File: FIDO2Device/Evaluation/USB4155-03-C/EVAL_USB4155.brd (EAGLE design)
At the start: 30 x 30 mm, 6 parts, among them CN1 USB4155-03-C, CN2 87520-0010BLF, CN3 IF_5PIN_H

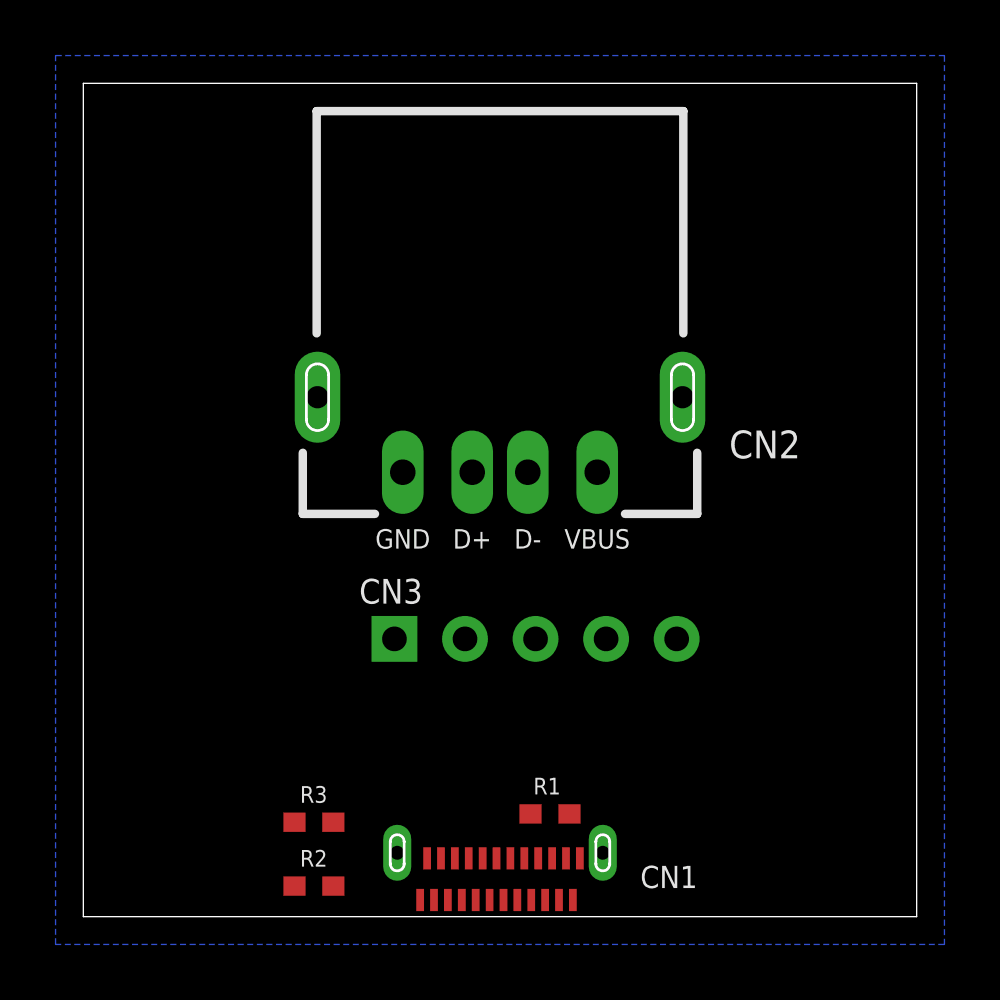
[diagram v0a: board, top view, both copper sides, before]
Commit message: レイアウトを更新
・信号線のViaを仮配置
・デザインルールを一部修正
（Drill＝0.2mm、Restring＝0.1mm、Clearance＝0.15mm）
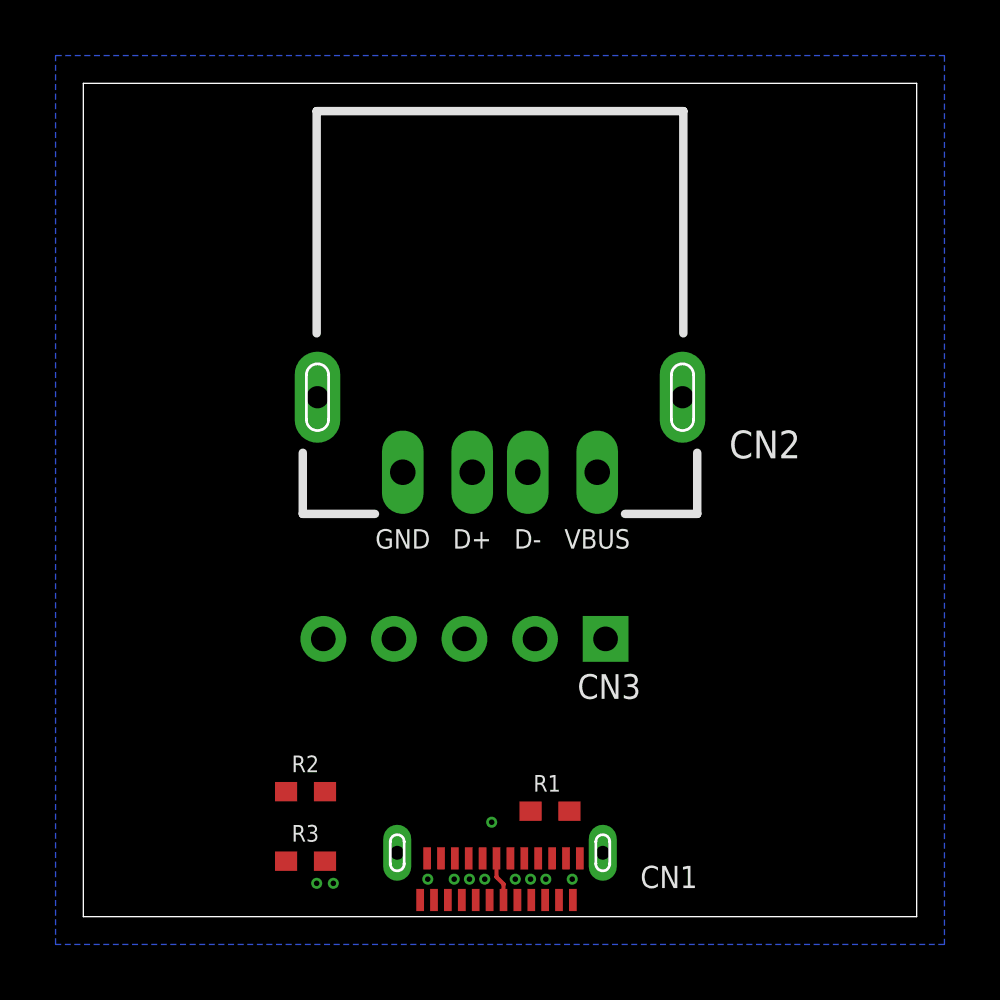
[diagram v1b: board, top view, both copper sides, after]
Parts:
- moved CN3 7.60 mm to (18.8, 10.0), turned to 180 degrees
- moved R2 3.41 mm to (8.00, 4.50), turned to 180 degrees
- moved R3 1.43 mm to (8.00, 2.00)
- moved R1 0.10 mm to (16.8, 3.80)
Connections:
- net N$1 renamed CC_1
- net N$2 renamed CC_2
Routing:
- net DN_C: track 0.00 -> 1.60 mm
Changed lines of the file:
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@@
 <param name="mtCopper" value="0.035mm 0.0175mm 0.035mm 0.035mm 0.035mm 0.035mm 0.035mm 0.035mm 0.035mm 0.035mm 0.035mm 0.035mm 0.035mm 0.035mm 0.0175mm 0.035mm"/>
 <param name="mtIsolate" value="1.5mm 1.1mm 0.2mm 0.15mm 0.2mm 0.15mm 0.2mm 0.15mm 0.2mm 0.15mm 0.2mm 0.15mm 0.2mm 0.15mm 0.2mm"/>
-<param name="mdWireWire" value="6mil"/>
-<param name="mdWirePad" value="6mil"/>
-<param name="mdWireVia" value="6mil"/>
-<param name="mdPadPad" value="6mil"/>
-<param name="mdPadVia" value="6mil"/>
-<param name="mdViaVia" value="6mil"/>
+<param name="mdWireWire" value="0.15mm"/>
+<param name="mdWirePad" value="0.15mm"/>
+<param name="mdWireVia" value="0.15mm"/>
+<param name="mdPadPad" value="0.15mm"/>
+<param name="mdPadVia" value="0.15mm"/>
+<param name="mdViaVia" value="0.15mm"/>
 <param name="mdSmdPad" value="0mil"/>
 <param name="mdSmdVia" value="0mil"/>
@@
 <param name="mdSmdStop" value="0mil"/>
 <param name="msWidth" value="6mil"/>
-<param name="msDrill" value="12mil"/>
+<param name="msDrill" value="0.2mm"/>
 <param name="msMicroVia" value="12mil"/>
 <param name="msBlindViaRatio" value="0.5"/>
@@
 <param name="rlMinPadBottom" value="10mil"/>
 <param name="rlMaxPadBottom" value="20mil"/>
-<param name="rlMinViaOuter" value="6mil"/>
+<param name="rlMinViaOuter" value="0.1mm"/>
 <param name="rlMaxViaOuter" value="20mil"/>
-<param name="rlMinViaInner" value="6mil"/>
+<param name="rlMinViaInner" value="0.1mm"/>
 <param name="rlMaxViaInner" value="20mil"/>
 <param name="rlMinMicroViaOuter" value="4mil"/>
@@
 </element>
 <element name="CN2" library="Connectors" package="87520-0010BLF" value="87520-0010BLF" x="15" y="16"/>
-<element name="CN3" library="Connectors" package="HEADER_5PIN" value="IF_5PIN_H" x="11.2" y="10"/>
-<element name="R1" library="Parts" package="R0402N" value="5.1k" x="16.8" y="3.7" smashed="yes" rot="R180">
-<attribute name="NAME" x="16.2" y="4.4" size="0.6" layer="25"/>
-<attribute name="VALUE" x="17.3" y="5" size="0.6" layer="27" rot="R180"/>
-</element>
-<element name="R2" library="Parts" package="R0402N" value="5.1k" x="8.3" y="1.1" smashed="yes">
-<attribute name="NAME" x="7.8" y="1.8" size="0.6" layer="25"/>
-<attribute name="VALUE" x="7.8" y="-0.2" size="0.6" layer="27"/>
-</element>
-<element name="R3" library="Parts" package="R0402N" value="0" x="8.3" y="3.4" smashed="yes">
-<attribute name="NAME" x="7.8" y="4.1" size="0.6" layer="25"/>
-<attribute name="VALUE" x="7.8" y="2.1" size="0.6" layer="27"/>
+<element name="CN3" library="Connectors" package="HEADER_5PIN" value="IF_5PIN_H" x="18.8" y="10" rot="R180"/>
+<element name="R1" library="Parts" package="R0402N" value="5.1k" x="16.8" y="3.8" smashed="yes" rot="R180">
+<attribute name="NAME" x="16.2" y="4.5" size="0.6" layer="25"/>
+<attribute name="VALUE" x="17.3" y="5.1" size="0.6" layer="27" rot="R180"/>
+</element>
+<element name="R2" library="Parts" package="R0402N" value="5.1k" x="8" y="4.5" smashed="yes" rot="R180">
+<attribute name="NAME" x="7.5" y="5.2" size="0.6" layer="25"/>
+<attribute name="VALUE" x="8.5" y="5.8" size="0.6" layer="27" rot="R180"/>
+</element>
+<element name="R3" library="Parts" package="R0402N" value="0" x="8" y="2" smashed="yes">
+<attribute name="NAME" x="7.5" y="2.7" size="0.6" layer="25"/>
+<attribute name="VALUE" x="7.5" y="0.7" size="0.6" layer="27"/>
 </element>
 </elements>
@@
 <vertex x="-1" y="-1"/>
 </polygon>
-<wire x1="17.625" y1="0.6" x2="17.875" y2="2.1" width="0" layer="19" extent="1-1"/>
-<wire x1="17.5" y1="3.7" x2="17.875" y2="2.1" width="0" layer="19" extent="1-1"/>
-<wire x1="12.375" y1="2.1" x2="17.5" y2="3.7" width="0" layer="19" extent="1-1"/>
-<wire x1="12.125" y1="0.6" x2="12.375" y2="2.1" width="0" layer="19" extent="1-1"/>
-<wire x1="7.6" y1="1.1" x2="12.125" y2="0.6" width="0" layer="19" extent="1-1"/>
-<wire x1="11.2" y1="10" x2="12.375" y2="2.1" width="0" layer="19" extent="1-1"/>
+<via x="17.6" y="1.35" extent="1-16" drill="0.2"/>
+<via x="12.4" y="1.35" extent="1-16" drill="0.2"/>
+<wire x1="17.6" y1="1.35" x2="17.875" y2="2.1" width="0" layer="19" extent="1-1"/>
+<wire x1="17.625" y1="0.6" x2="17.6" y2="1.35" width="0" layer="19" extent="1-1"/>
+<wire x1="12.375" y1="2.1" x2="12.4" y2="1.35" width="0" layer="19" extent="1-1"/>
+<wire x1="12.125" y1="0.6" x2="12.4" y2="1.35" width="0" layer="19" extent="1-1"/>
+<wire x1="17.5" y1="3.8" x2="17.875" y2="2.1" width="0" layer="19" extent="1-1"/>
+<wire x1="8.7" y1="4.5" x2="12.375" y2="2.1" width="0" layer="19" extent="1-1"/>
 </signal>
 <signal name="DP_C">
@@
 <contactref element="CN1" pad="A6"/>
 <contactref element="CN1" pad="B6"/>
-<wire x1="16.28" y1="10" x2="14" y2="16" width="0" layer="19" extent="1-1"/>
-<wire x1="15.375" y1="2.1" x2="16.28" y2="10" width="0" layer="19" extent="1-1"/>
-<wire x1="14.625" y1="0.6" x2="15.375" y2="2.1" width="0" layer="19" extent="1-1"/>
+<via x="15.55" y="1.35" extent="1-16" drill="0.2"/>
+<via x="14.45" y="1.35" extent="1-16" drill="0.2"/>
+<via x="14.7" y="3.4" extent="1-16" drill="0.2"/>
+<wire x1="13.72" y1="10" x2="14" y2="16" width="0" layer="19" extent="1-1"/>
+<wire x1="14.7" y1="3.4" x2="13.72" y2="10" width="0" layer="19" extent="1-1"/>
+<wire x1="15.375" y1="2.1" x2="14.7" y2="3.4" width="0" layer="19" extent="1-1"/>
+<wire x1="15.55" y1="1.35" x2="15.375" y2="2.1" width="0" layer="19" extent="1-1"/>
+<wire x1="14.45" y1="1.35" x2="15.55" y2="1.35" width="0" layer="19" extent="1-1"/>
+<wire x1="14.625" y1="0.6" x2="14.45" y2="1.35" width="0" layer="19" extent="1-1"/>
 </signal>
 <signal name="DN_C">
@@
 <contactref element="CN1" pad="A7"/>
 <contactref element="CN1" pad="B7"/>
-<wire x1="13.74" y1="10" x2="16" y2="16" width="0" layer="19" extent="1-1"/>
-<wire x1="14.875" y1="2.1" x2="13.74" y2="10" width="0" layer="19" extent="1-1"/>
-<wire x1="15.125" y1="0.6" x2="14.875" y2="2.1" width="0" layer="19" extent="1-1"/>
+<wire x1="15.125" y1="0.6" x2="15.125" y2="1.175" width="0.1524" layer="1"/>
+<wire x1="14.875" y1="2.1" x2="14.875" y2="1.425" width="0.1524" layer="1"/>
+<wire x1="14.875" y1="1.425" x2="15.125" y2="1.175" width="0.1524" layer="1"/>
+<wire x1="16.26" y1="10" x2="16" y2="16" width="0" layer="19" extent="1-1"/>
+<wire x1="14.875" y1="2.1" x2="16.26" y2="10" width="0" layer="19" extent="1-1"/>
 </signal>
 <signal name="VBUS_C">
@@
 <contactref element="CN1" pad="A9"/>
 <contactref element="CN1" pad="B4"/>
-<wire x1="18.82" y1="10" x2="18.5" y2="16" width="0" layer="19" extent="1-1"/>
-<wire x1="16.375" y1="2.1" x2="18.82" y2="10" width="0" layer="19" extent="1-1"/>
-<wire x1="16.125" y1="0.6" x2="16.375" y2="2.1" width="0" layer="19" extent="1-1"/>
-<wire x1="13.875" y1="2.1" x2="16.375" y2="2.1" width="0" layer="19" extent="1-1"/>
-<wire x1="13.625" y1="0.6" x2="13.875" y2="2.1" width="0" layer="19" extent="1-1"/>
+<via x="13.35" y="1.35" extent="1-16" drill="0.2"/>
+<via x="16.65" y="1.35" extent="1-16" drill="0.2"/>
+<wire x1="11.18" y1="10" x2="18.5" y2="16" width="0" layer="19" extent="1-1"/>
+<wire x1="13.875" y1="2.1" x2="11.18" y2="10" width="0" layer="19" extent="1-1"/>
+<wire x1="13.35" y1="1.35" x2="13.875" y2="2.1" width="0" layer="19" extent="1-1"/>
+<wire x1="13.625" y1="0.6" x2="13.35" y2="1.35" width="0" layer="19" extent="1-1"/>
+<wire x1="16.375" y1="2.1" x2="13.875" y2="2.1" width="0" layer="19" extent="1-1"/>
+<wire x1="16.65" y1="1.35" x2="16.375" y2="2.1" width="0" layer="19" extent="1-1"/>
+<wire x1="16.125" y1="0.6" x2="16.65" y2="1.35" width="0" layer="19" extent="1-1"/>
 </signal>
 <signal name="FG_C">
@@
 <contactref element="CN1" pad="FG1"/>
 <contactref element="CN1" pad="FG2"/>
-<wire x1="21.36" y1="10" x2="21.57" y2="18.7" width="0" layer="19" extent="1-1"/>
-<wire x1="18.7" y1="2.3" x2="21.36" y2="10" width="0" layer="19" extent="1-1"/>
-<wire x1="11.3" y1="2.3" x2="18.7" y2="2.3" width="0" layer="19" extent="1-1"/>
 <wire x1="8.43" y1="18.7" x2="21.57" y2="18.7" width="0" layer="19" extent="1-1"/>
-</signal>
-<signal name="N$1">
+<wire x1="8.64" y1="10" x2="8.43" y2="18.7" width="0" layer="19" extent="1-1"/>
+<wire x1="11.3" y1="2.3" x2="8.64" y2="10" width="0" layer="19" extent="1-1"/>
+<wire x1="18.7" y1="2.3" x2="11.3" y2="2.3" width="0" layer="19" extent="1-1"/>
+</signal>
+<signal name="CC_1">
 <contactref element="CN1" pad="A5"/>
 <contactref element="R3" pad="2"/>
 <contactref element="R1" pad="2"/>
-<wire x1="15.875" y1="2.1" x2="16.1" y2="3.7" width="0" layer="19" extent="1-1"/>
-<wire x1="9" y1="3.4" x2="15.875" y2="2.1" width="0" layer="19" extent="1-1"/>
-</signal>
-<signal name="N$2">
+<via x="16.1" y="1.35" extent="1-16" drill="0.2"/>
+<via x="9" y="1.2" extent="1-16" drill="0.2"/>
+<wire x1="15.875" y1="2.1" x2="16.1" y2="3.8" width="0" layer="19" extent="1-1"/>
+<wire x1="16.1" y1="1.35" x2="15.875" y2="2.1" width="0" layer="19" extent="1-1"/>
+<wire x1="9" y1="1.2" x2="15.875" y2="2.1" width="0" layer="19" extent="1-1"/>
+<wire x1="8.7" y1="2" x2="9" y2="1.2" width="0" layer="19" extent="1-1"/>
+</signal>
+<signal name="CC_2">
 <contactref element="CN1" pad="B5"/>
 <contactref element="R2" pad="2"/>
 <contactref element="R3" pad="1"/>
-<wire x1="9" y1="1.1" x2="14.125" y2="0.6" width="0" layer="19" extent="1-1"/>
-<wire x1="7.6" y1="3.4" x2="9" y2="1.1" width="0" layer="19" extent="1-1"/>
+<via x="13.9" y="1.35" extent="1-16" drill="0.2"/>
+<via x="8.4" y="1.2" extent="1-16" drill="0.2"/>
+<wire x1="13.9" y1="1.35" x2="14.125" y2="0.6" width="0" layer="19" extent="1-1"/>
+<wire x1="8.4" y1="1.2" x2="13.9" y2="1.35" width="0" layer="19" extent="1-1"/>
+<wire x1="7.3" y1="2" x2="8.4" y2="1.2" width="0" layer="19" extent="1-1"/>
+<wire x1="7.3" y1="4.5" x2="7.3" y2="2" width="0" layer="19" extent="1-1"/>
 </signal>
 </signals>

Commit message: レイアウトを更新
・差動信号を配線
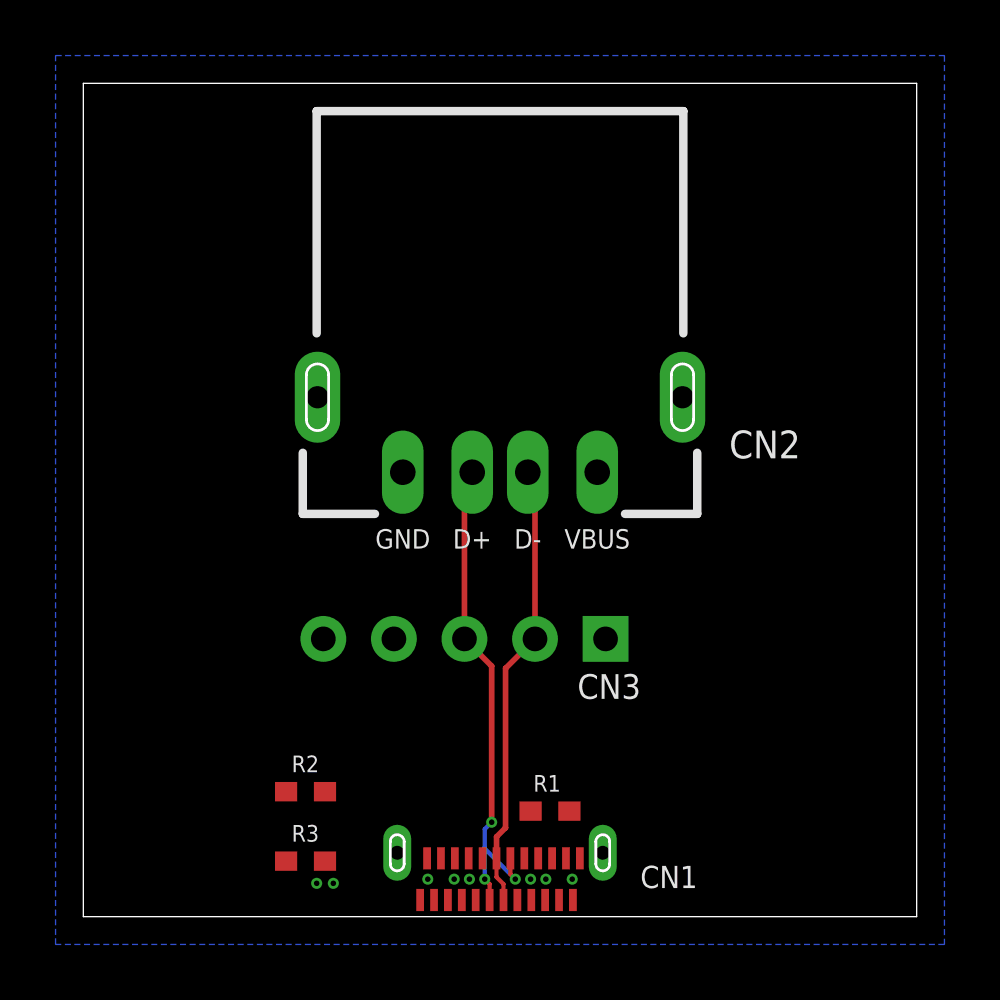
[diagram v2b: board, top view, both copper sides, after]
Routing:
- net DP_C: track 0.00 -> 18.5 mm
- net DN_C: track 1.60 -> 16.2 mm
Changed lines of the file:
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@@
 <via x="14.45" y="1.35" extent="1-16" drill="0.2"/>
 <via x="14.7" y="3.4" extent="1-16" drill="0.2"/>
-<wire x1="13.72" y1="10" x2="14" y2="16" width="0" layer="19" extent="1-1"/>
-<wire x1="14.7" y1="3.4" x2="13.72" y2="10" width="0" layer="19" extent="1-1"/>
-<wire x1="15.375" y1="2.1" x2="14.7" y2="3.4" width="0" layer="19" extent="1-1"/>
-<wire x1="15.55" y1="1.35" x2="15.375" y2="2.1" width="0" layer="19" extent="1-1"/>
-<wire x1="14.45" y1="1.35" x2="15.55" y2="1.35" width="0" layer="19" extent="1-1"/>
-<wire x1="14.625" y1="0.6" x2="14.45" y2="1.35" width="0" layer="19" extent="1-1"/>
+<wire x1="14.625" y1="0.6" x2="14.625" y2="1.175" width="0.1524" layer="1"/>
+<wire x1="15.55" y1="1.35" x2="15.375" y2="1.525" width="0.1524" layer="1"/>
+<wire x1="15.375" y1="1.525" x2="15.375" y2="2.1" width="0.1524" layer="1"/>
+<wire x1="14.45" y1="1.35" x2="14.625" y2="1.175" width="0.1524" layer="1"/>
+<wire x1="14.7" y1="3.4" x2="14.7" y2="9.02" width="0.2032" layer="1"/>
+<wire x1="14.7" y1="9.02" x2="13.72" y2="10" width="0.2032" layer="1"/>
+<wire x1="14.7" y1="3.4" x2="14.45" y2="3.15" width="0.1524" layer="16"/>
+<wire x1="14.45" y1="3.15" x2="14.45" y2="2.5" width="0.1524" layer="16"/>
+<wire x1="14.45" y1="2.45" x2="14.45" y2="1.35" width="0.1524" layer="16"/>
+<wire x1="15.55" y1="1.35" x2="14.45" y2="2.45" width="0.1524" layer="16"/>
+<wire x1="14.45" y1="2.45" x2="14.45" y2="2.5" width="0.1524" layer="16"/>
+<wire x1="13.72" y1="10" x2="13.72" y2="15.72" width="0.2032" layer="1"/>
+<wire x1="13.72" y1="15.72" x2="14" y2="16" width="0.2032" layer="1"/>
 </signal>
 <signal name="DN_C">
@@
 <wire x1="14.875" y1="2.1" x2="14.875" y2="1.425" width="0.1524" layer="1"/>
 <wire x1="14.875" y1="1.425" x2="15.125" y2="1.175" width="0.1524" layer="1"/>
-<wire x1="16.26" y1="10" x2="16" y2="16" width="0" layer="19" extent="1-1"/>
-<wire x1="14.875" y1="2.1" x2="16.26" y2="10" width="0" layer="19" extent="1-1"/>
+<wire x1="14.875" y1="2.1" x2="14.875" y2="2.875" width="0.2032" layer="1"/>
+<wire x1="14.875" y1="2.875" x2="15.2" y2="3.2" width="0.2032" layer="1"/>
+<wire x1="15.2" y1="3.2" x2="15.2" y2="8.94" width="0.2032" layer="1"/>
+<wire x1="15.2" y1="8.94" x2="16.26" y2="10" width="0.2032" layer="1"/>
+<wire x1="16.26" y1="10" x2="16.26" y2="15.74" width="0.2032" layer="1"/>
+<wire x1="16.26" y1="15.74" x2="16" y2="16" width="0.2032" layer="1"/>
 </signal>
 <signal name="VBUS_C">

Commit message: レイアウトを更新
・電源／信号を配線
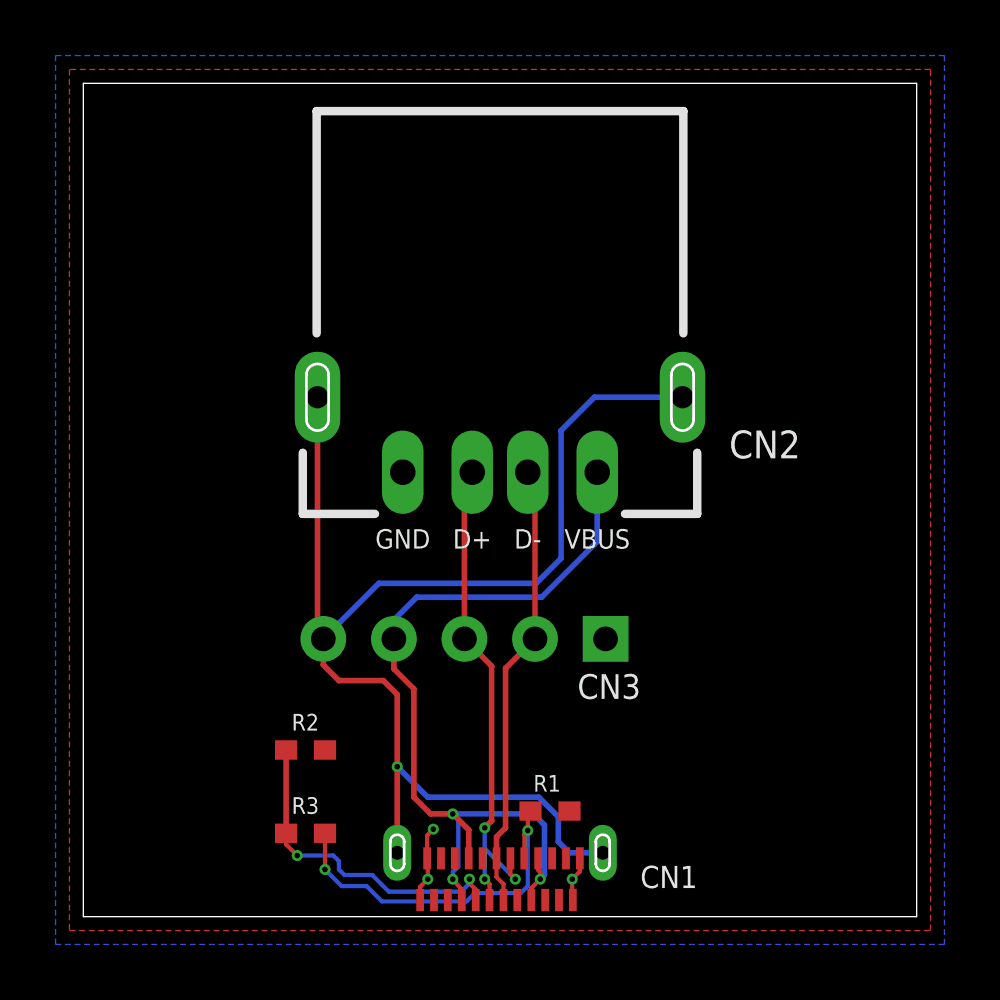
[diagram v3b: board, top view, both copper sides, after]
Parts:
- moved R2 1.50 mm to (8.00, 6.00)
- moved R3 1.00 mm to (8.00, 3.00)
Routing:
- net FG_C: track 0.00 -> 47.0 mm, vias 0 -> 1
- net VBUS_C: track 0.00 -> 31.7 mm, vias 2 -> 3
- net CC_1: track 0.00 -> 13.1 mm
- net CC_2: track 0.00 -> 12.0 mm
- net 0V: track 0.00 -> 4.39 mm, vias 2 -> 3
- added copper zone on layer 1, net 0V
